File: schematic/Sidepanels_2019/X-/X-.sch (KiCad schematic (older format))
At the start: 33 parts, among them J1 Conn_01x04, J2 Conn_01x02

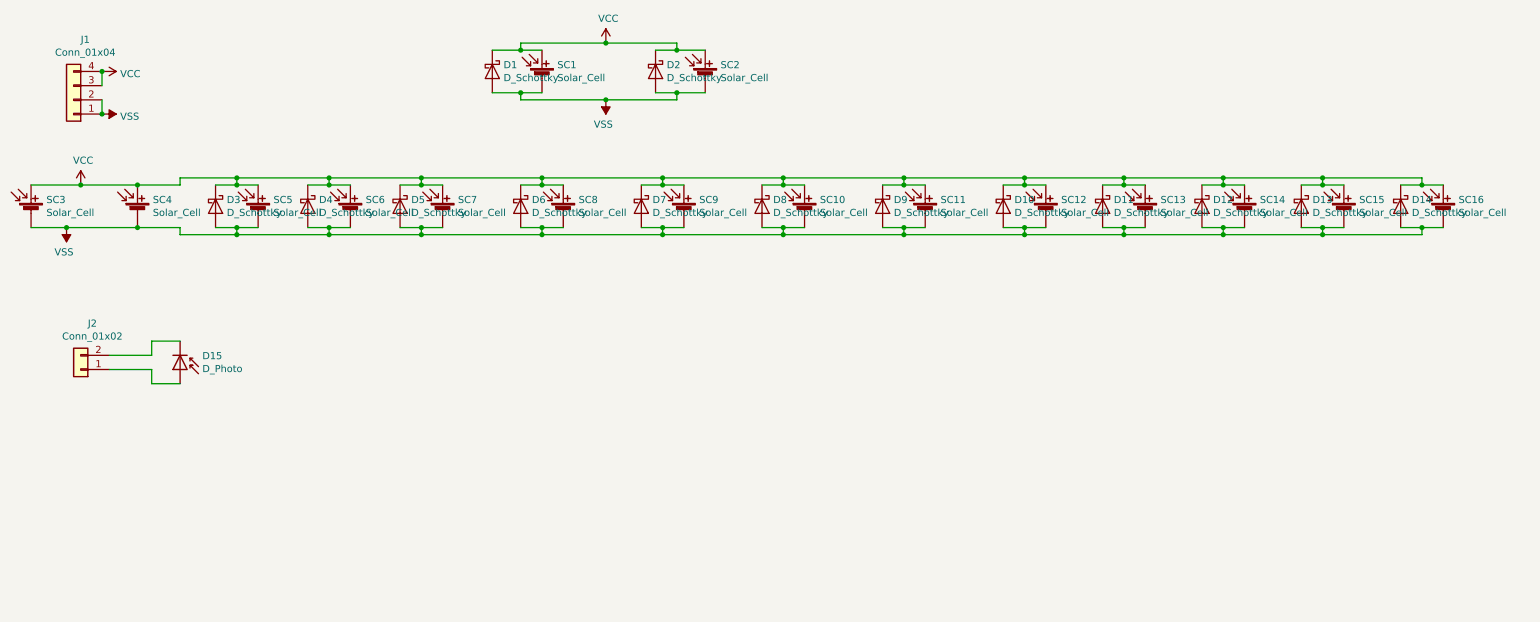
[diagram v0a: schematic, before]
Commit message: First attempt at modifying to all Spectrolabs.  NOT COMPLETE
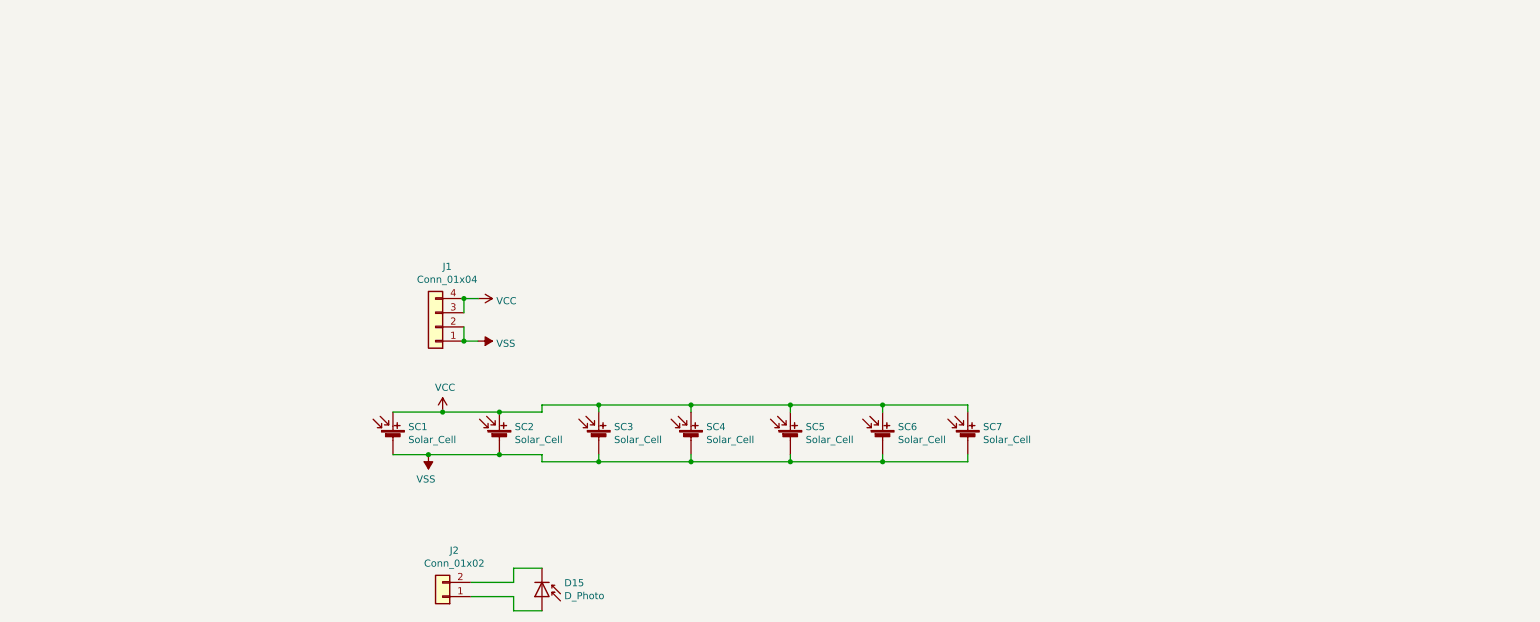
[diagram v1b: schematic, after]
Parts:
- removed D1, D10, D11, D12, D13, D14, D2, D3, D4, D5, D6, D7, D8, D9: D_Schottky, CySat footprints:Toshiba_CUS08F30, symbol Device:D_Schottky
- removed SC1, SC2: Solar_Cell, CySat footprints:ISS_SolarCell, symbol Device:Solar_Cell
- removed SC10, SC11, SC12, SC13, SC14, SC15, SC16, SC8, SC9: Solar_Cell, CySat footprints:TriSelectSolarPanel, symbol Device:Solar_Cell
- added SC3, SC4: Solar_Cell, CySat_Solar:Spectrolab, symbol Device:Solar_Cell
- D15: footprint CySat footprints:Sun_Sensor -> Diode_SMD:D_0805_2012Metric
- SC1: renamed from SC3; footprint CySat footprints:Spectrolab -> CySat_Solar:Spectrolab
- SC2: renamed from SC4; footprint CySat footprints:Spectrolab -> CySat_Solar:Spectrolab
- SC5, SC6, SC7: footprint CySat footprints:TriSelectSolarPanel -> CySat_Solar:Spectrolab
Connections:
- net VCC: now also SC3.1 (+), SC4.1 (+)
- net VSS: now also SC3.2 (-), SC4.2 (-)
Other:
- moved on the sheet: D15, J1, J2, SC1, SC2
